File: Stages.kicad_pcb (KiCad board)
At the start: 2 copper layers, 69 x 100 mm, 223 parts, among them IC1 TLC59281, IC10 MCP6002, IC11 LM4040DBZ-2.5, IC12 TL074, IC13 TL074, IC14 TL074, IC2 R-78E3.3-0.5, IC3 4051, IC4 DAC8168, IC5 STM32F373RBTx, IC6 4051, IC7 LD2981ABU33, IC8 MCP6002, IC9 MCP6002, J1 -8.1V to 8.1V, J10 WQP-PJ301M-12_JACK, J11 WQP-PJ301M-12_JACK, J12 WQP-PJ301M-12_JACK, J13 -8.1V to 8.1V, J14 -8.1V to 8.1V, J15 -8.1V to 8.1V, J16 -8.1V to 8.1V, J17 -8.1V to 8.1V, J18 -8.1V to 8.1V, J2 -8.1V to 8.1V, J3 -8.1V to 8.1V, J4 -8.1V to 8.1V, J5 -8.1V to 8.1V, J6 -8.1V to 8.1V, J7 WQP-PJ301M-12_JACK, J8 WQP-PJ301M-12_JACK, J9 WQP-PJ301M-12_JACK, Q1 8MHz, Q2 MMBT3904, Q3 MMBT3904, Q4 MMBT3904, Q5 MMBT3904, Q6 MMBT3904, Q7 MMBT3904, SW1 SW_Push_4pin, SW2 SW_Push_4pin, SW3 SW_Push_4pin, SW4 SW_Push_4pin, SW5 SW_Push_4pin, SW6 SW_Push_4pin

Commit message: Tidy up Ground outes
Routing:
- net 4051GND: track 341.6 -> 358.5 mm, vias 69 -> 73
- net LEFT_RX: track 46.5 -> 48.4 mm
- net LEFT_TX: track 52.8 -> 54.6 mm

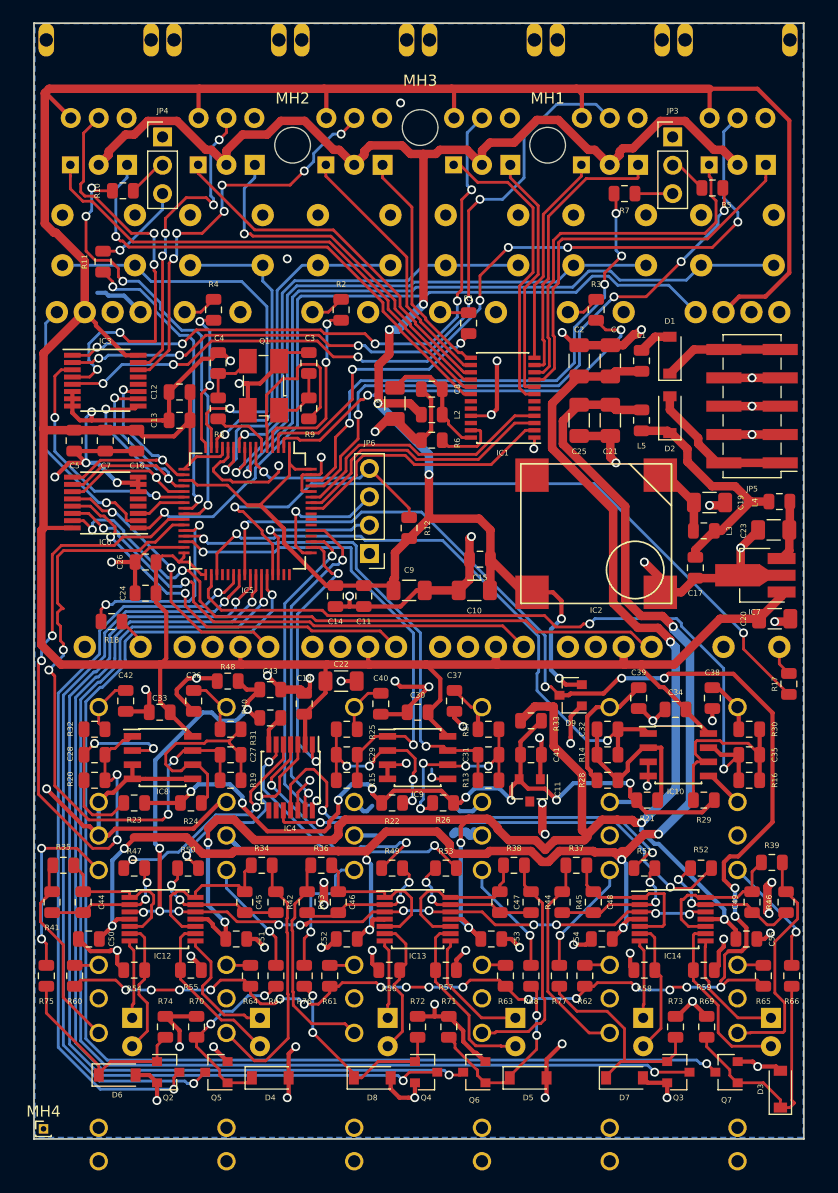
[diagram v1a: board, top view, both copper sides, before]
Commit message: Fixed Component pinouts
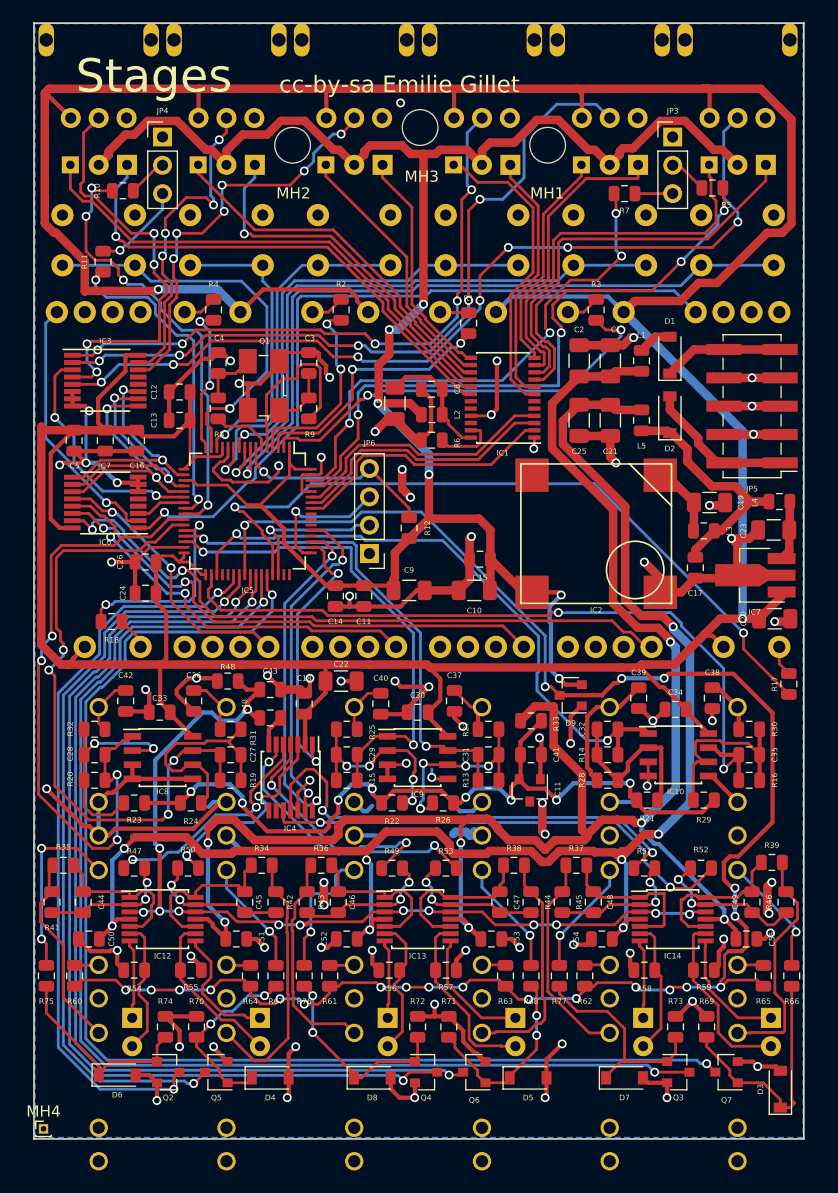
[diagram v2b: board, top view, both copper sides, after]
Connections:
- R78 pad 1: +3V3_A -> 4051GND
- R78 pad 3: 4051GND -> +3V3_A
- R79 pad 1: +3V3_A -> 4051GND
- R79 pad 3: 4051GND -> +3V3_A
- R80 pad 1: +3V3_A -> 4051GND
- R80 pad 3: 4051GND -> +3V3_A
- R81 pad 1: +3V3_A -> 4051GND
- R81 pad 3: 4051GND -> +3V3_A
- R82 pad 1: +3V3_A -> 4051GND
- R82 pad 3: 4051GND -> +3V3_A
- R83 pad 1: +3V3_A -> 4051GND
- R83 pad 3: 4051GND -> +3V3_A
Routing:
- net +3V3_A: track 318.5 -> 394.8 mm, vias 0 -> 2
- net 4051GND: track 358.5 -> 351.0 mm, vias 73 -> 74
- net LEFT_TX: track 54.6 -> 58.1 mm
- net SW_MODE_6: track 38.2 -> 35.9 mm
- net RIGHT_TX: track 27.4 -> 29.0 mm
- net Net-(IC1-Pad9): track 36.0 -> 37.4 mm
- net Net-(IC1-Pad10): track 33.7 -> 35.1 mm
- net Net-(IC1-Pad11): track 25.0 -> 26.4 mm
- net LEFT_RX: track 48.4 -> 47.3 mm
- net Net-(IC6-Pad1): track 68.2 -> 67.1 mm
- net STAGE_LED_4: track 16.6 -> 17.6 mm
- net Net-(IC1-Pad12): track 19.0 -> 20.0 mm
- net Net-(IC3-Pad4): track 37.0 -> 37.7 mm
- net Net-(IC3-Pad15): track 28.4 -> 29.0 mm
- net SW_MODE_1: track 65.0 -> 64.3 mm
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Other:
- board text added: "Stages"
- board text added: "cc-by-sa Emilie Gillet"

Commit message: Submitted Design
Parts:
- moved R12 1.58 mm to (135.5, 96.6)
- moved JP6 1.44 mm to (132.5, 97.5)
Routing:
- net RESET: track 18.4 -> 20.8 mm
- net SWDIO: track 13.4 -> 14.8 mm
- net SWCLK: track 12.3 -> 13.7 mm
